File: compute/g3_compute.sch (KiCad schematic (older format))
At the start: 60 parts, among them J101 Pi_Connector, J102 Temp_Connector_1x4, J103 53261-1071, J104 53261-1071, J105 CONSMA001-SMD-G, J106 53261-1071, J107 CONSMA001-SMD-G, J108 Conn_01x07_Male, Q101 PBSS4140DPN, U101 PA1616D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

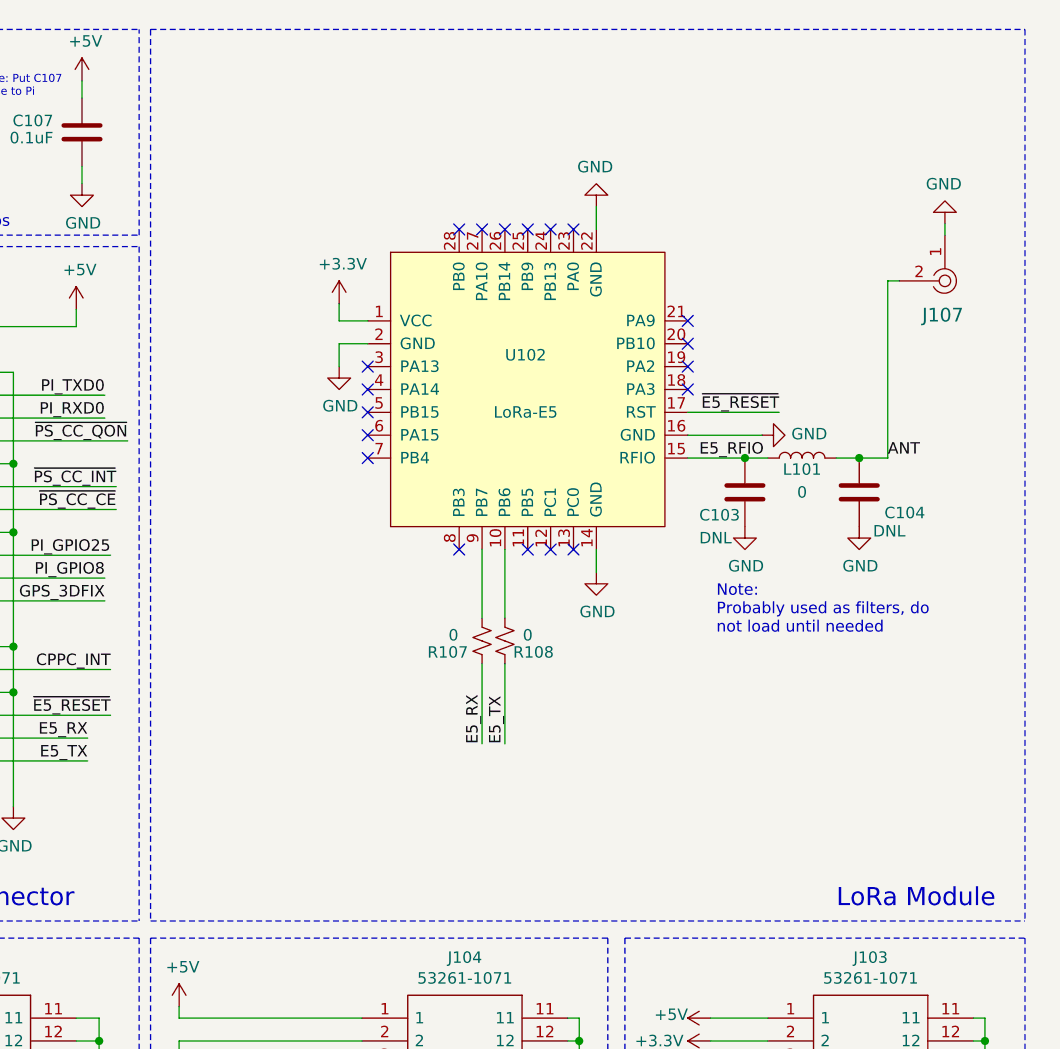
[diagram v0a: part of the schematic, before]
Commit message: Added the backup LoRa module again
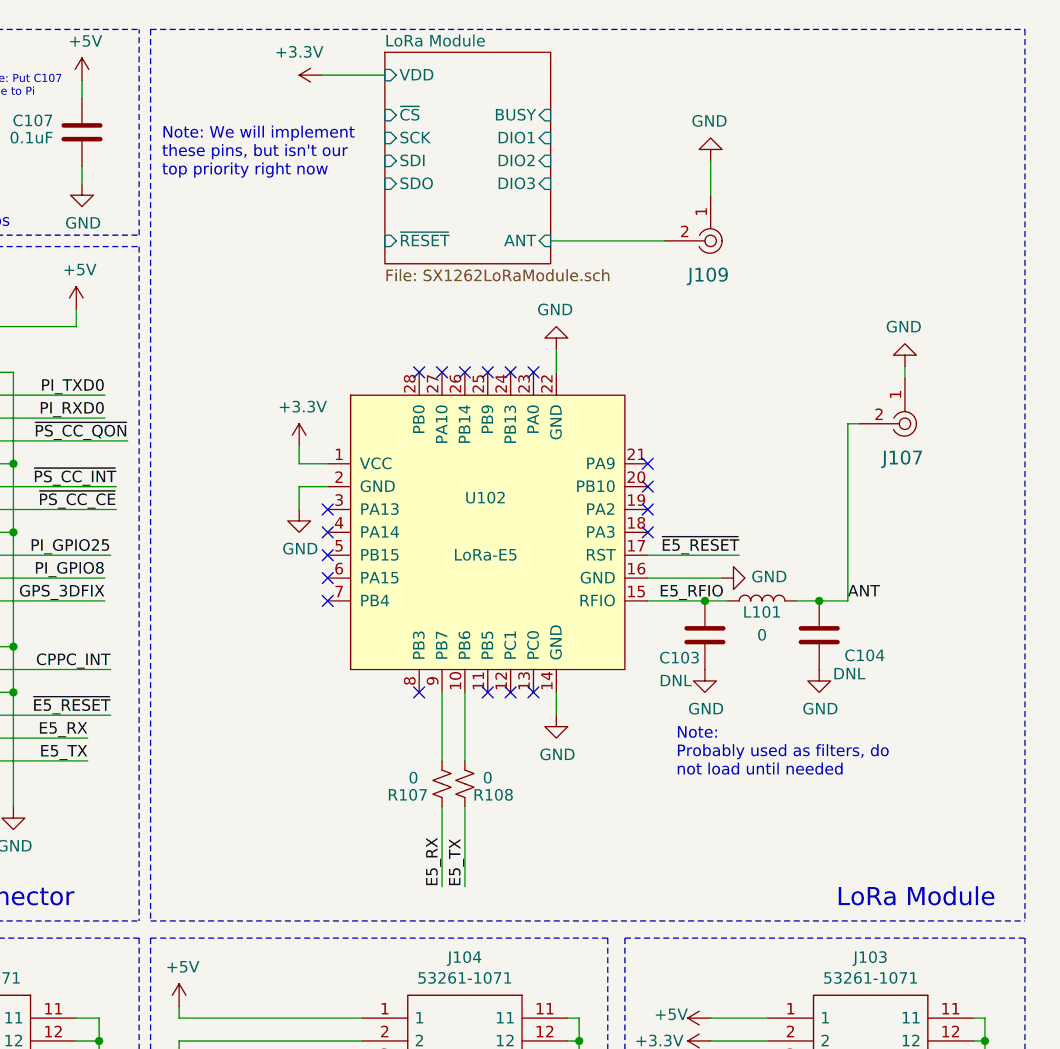
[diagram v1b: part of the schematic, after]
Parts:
- added J109: CONSMA001-SMD-G, digikey-footprints:RF_SMA_Receptical_Vertical_CONSMA001-SMD-G, symbol dk_Coaxial-Connectors-RF:CONSMA001-SMD-G
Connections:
- net GND: now also J109.1
- new net LoRa Module/ANT: J109.2
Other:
- note added: "Note: We will implement\nthese pins, but isn't our\ntop priority right now"
- moved on the sheet: C103, C104, J107, L101, R107, R108, U102

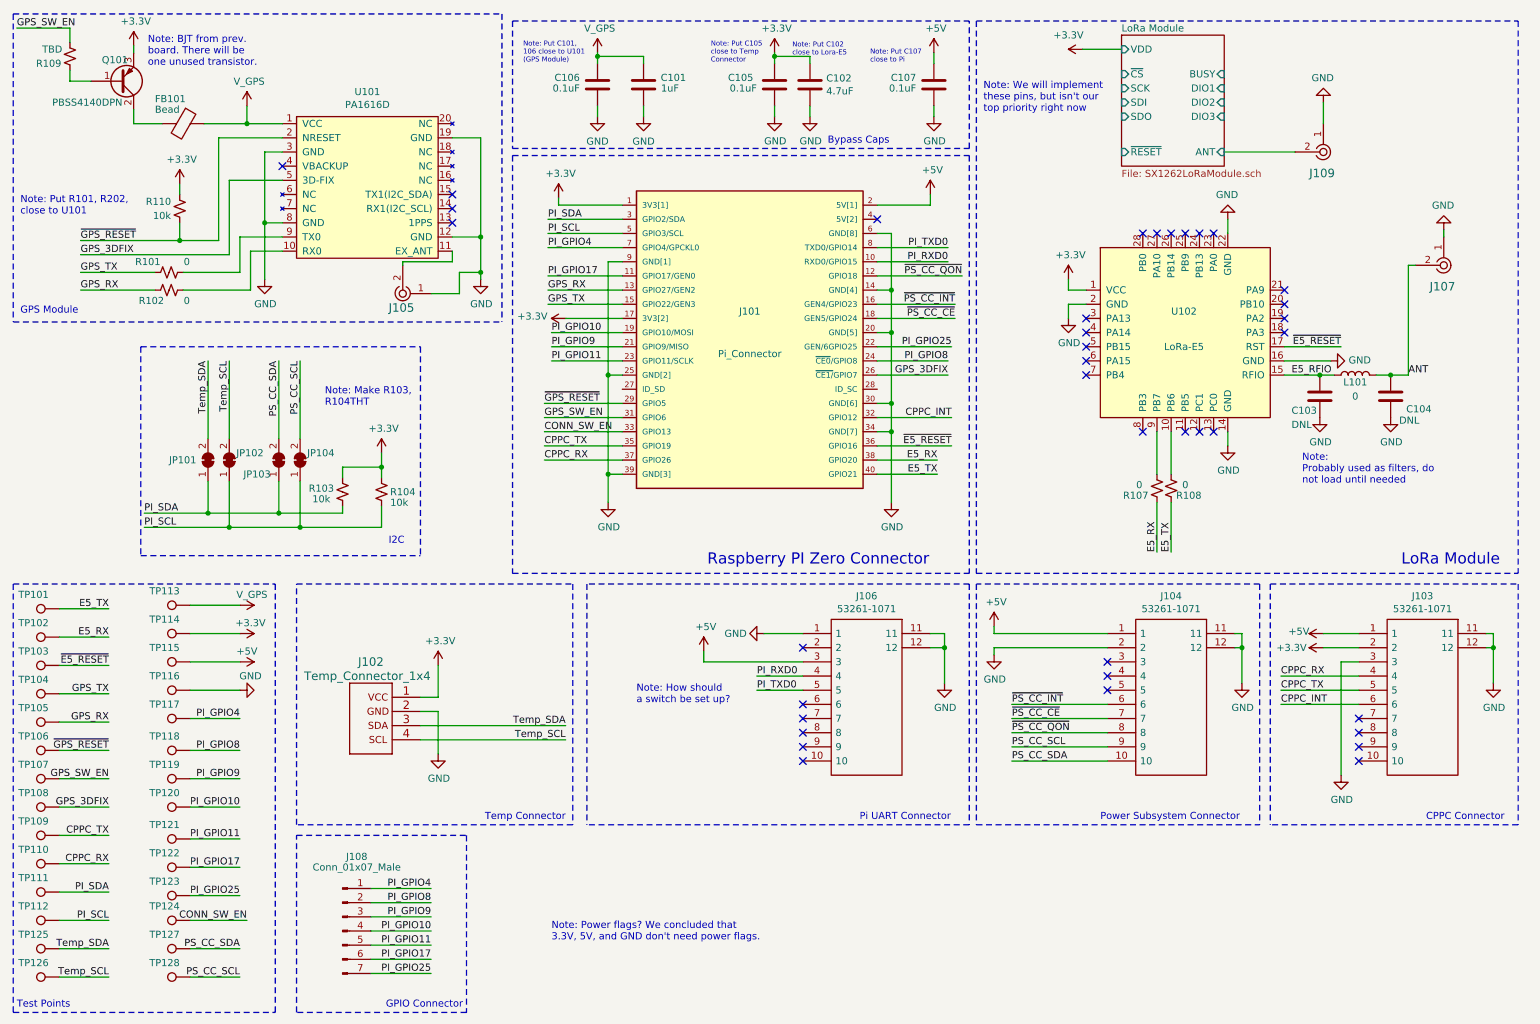
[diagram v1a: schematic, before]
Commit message: added some minor changes according to Perch feedback
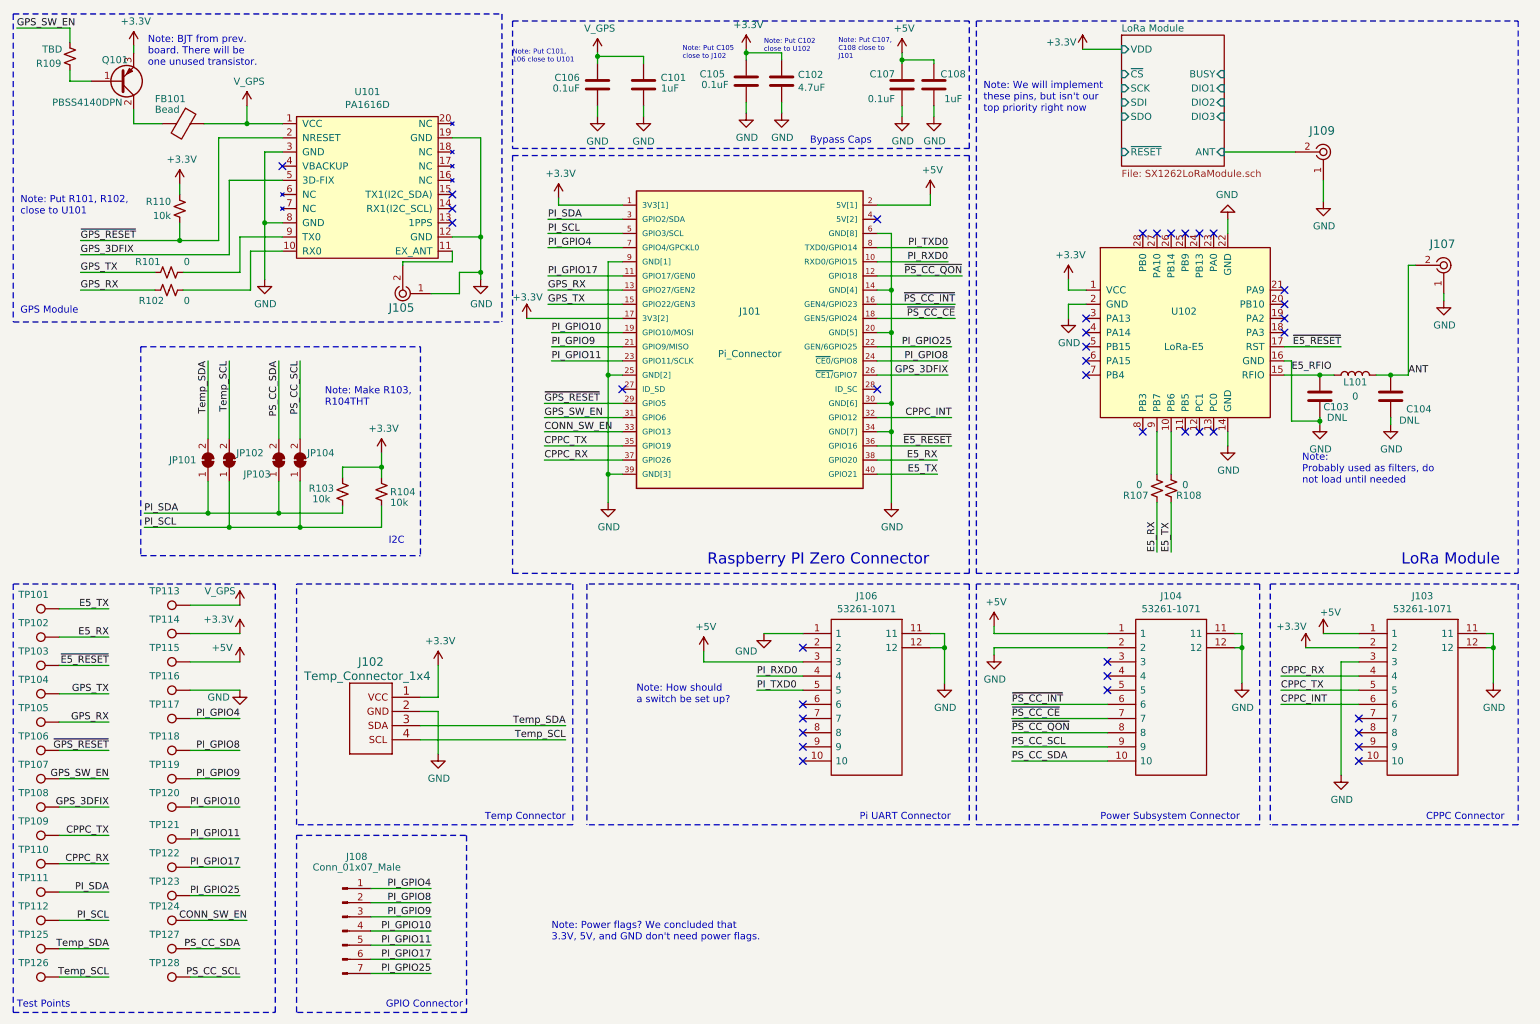
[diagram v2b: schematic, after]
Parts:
- added C108: 1uF, Capacitor_SMD:C_0402_1005Metric_Pad0.74x0.62mm_HandSolder, symbol Device:C
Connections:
- net +5V: now also C108.2
- net GND: now also C108.1
- net E5_RFIO: no longer names the net of C103.1, L101.1, U102.15 (RFIO)
- no-connect marks 37 -> 39
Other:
- note added: "Note: Put C101,\n106 close to U101"
- note added: "Note: Put C102\nclose to U102"
- note added: "Note: Put C105\nclose to J102\n"
- note added: "Note: Put C107,\nC108 close to\nJ101"
- note added: "Note: Put R101, R102, \nclose to U101\n"
- note removed: "Note: Put C101,\n106 close to U101\n(GPS Module)"
- note removed: "Note: Put C102\nclose to Lora-E5"
- note removed: "Note: Put C105\nclose to Temp\nConnector"
- note removed: "Note: Put C107\nclose to Pi"
- note removed: "Note: Put R101, R202, \nclose to U101\n"
- moved on the sheet: C102, C105, C107, J107, J109

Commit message: Made NC pins more consistent on compute schematic
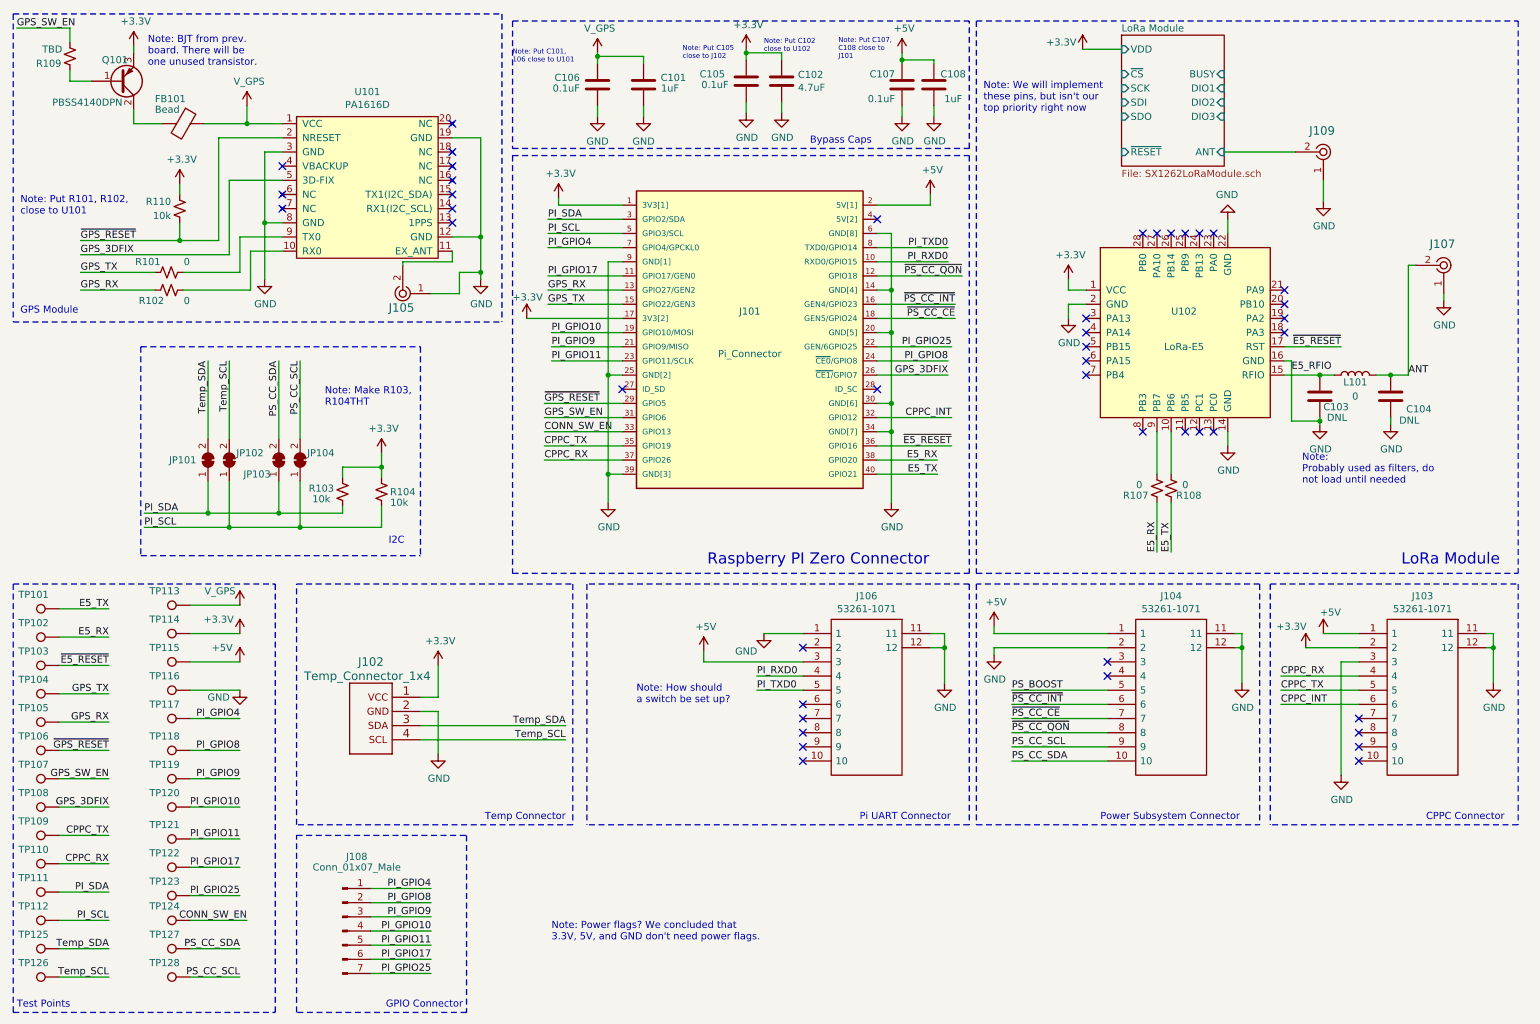
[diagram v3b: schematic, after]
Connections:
- net PS_BOOST: now reaches J104.5
- no-connect marks 39 -> 44
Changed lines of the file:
@@
 Wire Wire Line
 	7450 5000 7450 5050
-NoConn ~ 8250 5300
 NoConn ~ 8250 5200
 NoConn ~ 8250 5100
@@
 Wire Wire Line
 	7025 1175 7025 1250
+Wire Wire Line
+	8250 5300 7575 5300
+Text Label 7575 5300 0    50   ~ 0
+PS_BOOST
+NoConn ~ 3625 1600
+NoConn ~ 3625 1700
+NoConn ~ 3625 1500
+NoConn ~ 3625 1300
+NoConn ~ 2425 1800
+NoConn ~ 2425 1900
 $EndSCHEMATC

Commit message: Removed UART Resitors, Fixed I2C pull up resistors, changed Pi UART Connector to standard male header
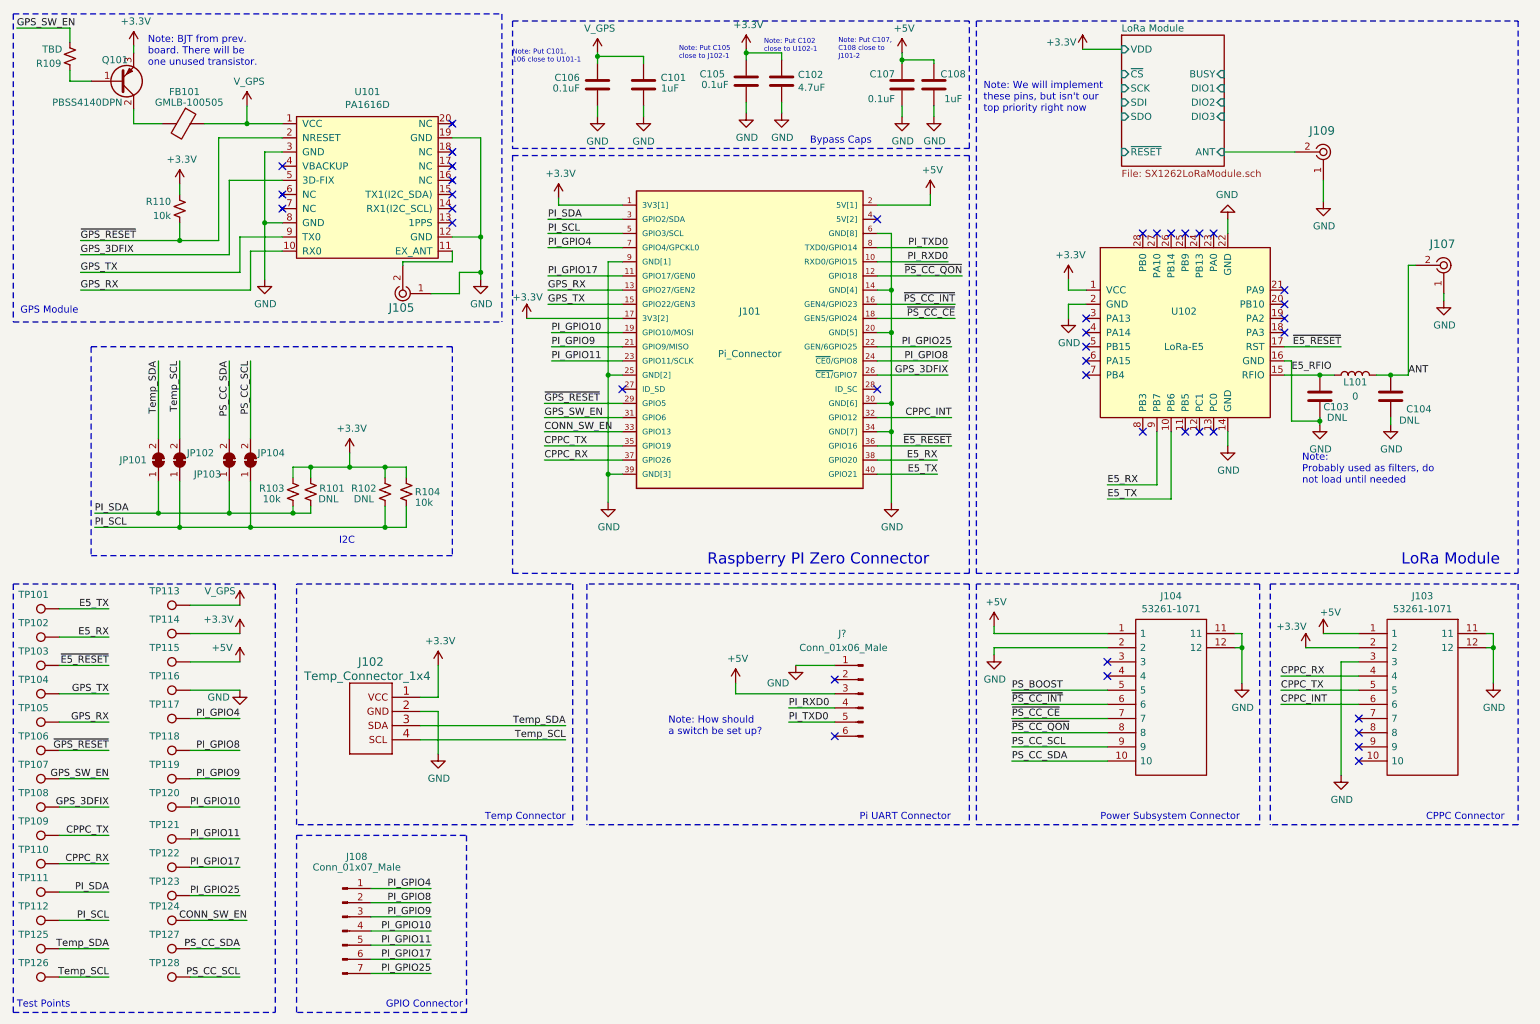
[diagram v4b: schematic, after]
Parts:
- removed J106: 53261-1071, Perch:532611071_Molex, symbol 53261-1071:53261-1071
- removed R107, R108: 0, Resistor_SMD:R_0402_1005Metric_Pad0.72x0.64mm_HandSolder, symbol Device:R_Small_US
- added J?: Conn_01x06_Male, Connector_PinHeader_2.54mm:PinHeader_1x06_P2.54mm_Vertical, symbol Connector:Conn_01x06_Male
- FB101: value Bead -> GMLB-100505; Description (none) -> Ferrite Bead; MFN (none) -> Mag Layers; MFP (none) -> GMLB-100505-0600A; S1PL (none) -> https://www.digikey.com/en/products/detail/mag-layers/GMLB-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; S1PN (none) -> 2669-GMLB-100505-0600A
- R101, R102: value 0 -> DNL; Description 0 Ohm resistor -> 0 Resistor; S1PN 13-AC0402FR-070 -> 13-AC0402FR-070RL; S2PL https://www.mouser.com/ProductDetail/YAGEO/AC0402FR-070RL?q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 -> (none); S2PN 603-AC0402FR-070RL -> (none)
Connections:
- net +3V3: now also R101.2, R102.2
- net +5V: now also J?.3 (Pin_3)
- net E5_RX: now also U102.9 (PB7)
- net E5_TX: now also U102.10 (PB6)
- net GND: now also J?.1 (Pin_1)
- net GPS_RX: now also U101.10 (RX0); no longer R102.2
- net GPS_TX: now also U101.9 (TX0); no longer R101.2
- net PI_RXD0: now also J?.4 (Pin_4)
- net PI_SCL: now also R102.1
- net PI_SDA: now also R101.1
- net PI_TXD0: now also J?.5 (Pin_5)
- no-connect marks 44 -> 40
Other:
- note added: "Note: Put C101,\n106 close to U101-1"
- note added: "Note: Put C102\nclose to U102-1"
- note added: "Note: Put C105\nclose to J102-1\n"
- note added: "Note: Put C107,\nC108 close to\nJ101-2"
- note added: "\n"
- note removed: "Note: Make R103, \nR104THT\n"
- note removed: "Note: Power flags? We concluded that\n3.3V, 5V, and GND don't need power flags."
- note removed: "Note: Put C101,\n106 close to U101"
- note removed: "Note: Put C102\nclose to U102"
- note removed: "Note: Put C105\nclose to J102\n"
- note removed: "Note: Put C107,\nC108 close to\nJ101"
- note removed: "Note: Put R101, R102, \nclose to U101\n"
- moved on the sheet: JP101, JP102, JP103, JP104, R103, R104
